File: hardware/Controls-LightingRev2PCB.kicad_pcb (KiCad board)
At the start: 2 copper layers, 54.5 x 53.5 mm, 52 parts, among them IC1 LM74502HDDFR, IC3 ACS724LLCTR-05AU-T, IC4 ACS724LLCTR-05AU-T, IC5 TLV70433DBVT, IC6 ACS724LLCTR-05AU-T, J1 53307-2471, J3 Conn_02x05_Top_Bottom, J4 Conn_01x02, J5 Conn_01x02, J6 Conn_01x03, Q1 NVMFWS1D7N04XMT1G, Q3 IRLML0030, Q4 NVMFWS1D7N04XMT1G, Q5 IRLML0030, U5 SN74LV1T34DBV

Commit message: Layout Review
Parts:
- moved 24V_TP1 93.4 mm to (224.9, 104.7)
- moved LVGND_TP1 86.5 mm to (219.1, 89.3)
- moved GPIO_Addr5v2 73.8 mm to (215.9, 135.3), turned to 90 degrees
- moved GPIO_BPS2 70.4 mm to (208.0, 136.0), turned to 90 degrees
- moved GPIO_Norm1 68.1 mm to (201.8, 135.7), turned to 90 degrees
- moved BPS_Sense2 67.0 mm to (224.0, 119.7), turned to -90 degrees
- moved Norm_Sense1 51.7 mm to (224.0, 112.3), turned to -90 degrees
- moved Addr_Sense2 50.4 mm to (220.9, 93.5)
- moved C24 41.2 mm to (226.7, 96.6), turned to 0 degrees
- moved C21 35.1 mm to (225.9, 99.9), turned to -90 degrees
- moved IC6 32.3 mm to (221.3, 98.6), turned to 0 degrees
- moved C20 29.6 mm to (216.7, 98.7), turned to 90 degrees
- moved C3 20.6 mm to (219.6, 111.0), turned to 0 degrees
- moved C2 16.3 mm to (218.8, 114.3), turned to -90 degrees
- moved R15 13.9 mm to (210.9, 132.7), turned to 0 degrees
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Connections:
- J1 pad 11: ADDR_Sense -> NORMAL_Sense
- J1 pad 13: NORMAL_Sense -> BPS_Sense
- J1 pad 15: BPS_Sense -> GPIO_Addr
- J1 pad 9: GPIO_Addr -> ADDR_Sense
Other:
- outline, holes or cut-outs redrawn

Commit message: Some routing
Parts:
- moved Addr_Sense2 36.3 mm to (232.9, 127.7)
- moved C20 30.1 mm to (213.5, 128.6)
- moved C24 30.1 mm to (223.4, 126.6)
- moved C21 30.1 mm to (222.7, 129.9)
- moved IC6 30.1 mm to (218.1, 128.6)
- moved C15 13.9 mm to (215.2, 108.3)
- moved R12 13.4 mm to (202.0, 109.7)
- moved C12 13.4 mm to (206.0, 106.4)
- moved C17 13.4 mm to (216.0, 105.7)
- moved IC4 13.4 mm to (210.6, 107.7)
- moved Q5 13.4 mm to (204.8, 109.7)
- moved R7 12.6 mm to (219.6, 95.5), turned to 0 degrees
- moved BPS_Sense2 12.4 mm to (224.1, 107.3)
- moved LVPWR1 10.8 mm to (221.9, 96.3), turned to 90 degrees
- moved C6 9.29 mm to (219.5, 97.1), turned to 0 degrees
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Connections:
- 24V_TP1 pad 1: Addressable_PWR -> +24V
- C1 pad 1: Addressable_GND -> GND
- C10 pad 1: Addressable_GND -> GND
- C10 pad 2: Addressable_PWR -> +24V
- C12 pad 1: Addressable_GND -> GND
- C12 pad 2: Addressable_PWR -> +24V
- C15 pad 2: Addressable_GND -> GND
- C17 pad 2: Addressable_GND -> GND
- C19 pad 1: Addressable_GND -> GND
- C2 pad 2: Addressable_GND -> GND
- C20 pad 1: Addressable_GND -> GND
- C20 pad 2: Addressable_PWR -> +24V
- C21 pad 2: Addressable_GND -> GND
- C22 pad 1: Addressable_GND -> GND
- C22 pad 2: Addressable_PWR -> +24V
- C23 pad 1: Addressable_GND -> GND
- C24 pad 2: Addressable_GND -> GND
- C3 pad 2: Addressable_GND -> GND
- C4 pad 2: Addressable_GND -> GND
- C6 pad 1: Addressable_PWR -> +24V
- C6 pad 2: Addressable_GND -> GND
- C7 pad 1: Addressable_PWR -> +24V
- C7 pad 2: Addressable_GND -> GND
- C8 pad 1: Addressable_PWR -> +24V
- C8 pad 2: Addressable_GND -> GND
- C9 pad 2: Addressable_GND -> GND
- D1 pad 2: Addressable_GND -> GND
- IC1 pad 2: Addressable_GND -> GND
- IC3 pad 1: Addressable_PWR -> +24V
- IC3 pad 2: Addressable_PWR -> +24V
- IC3 pad 3: Normal_GND -> Net-(IC3-IP-_1)
- IC3 pad 4: Normal_GND -> Net-(IC3-IP-_1)
- IC3 pad 5: Addressable_GND -> GND
- IC4 pad 1: Addressable_PWR -> +24V
- IC4 pad 2: Addressable_PWR -> +24V
- IC4 pad 3: Strobe_GND -> Net-(IC4-IP-_1)
- IC4 pad 4: Strobe_GND -> Net-(IC4-IP-_1)
- IC4 pad 5: Addressable_GND -> GND
- IC5 pad 1: Addressable_GND -> GND
- IC5 pad 2: Addressable_PWR -> +24V
- IC6 pad 1: Addressable_PWR -> +24V
- IC6 pad 2: Addressable_PWR -> +24V
- IC6 pad 3: Addressable_GND -> Net-(IC6-IP-_1)
- IC6 pad 4: Addressable_GND -> Net-(IC6-IP-_1)
- IC6 pad 5: Addressable_GND -> GND
- J1 pad 1: Addressable_GND -> GND
- J1 pad 24: Addressable_PWR -> +24V
- J1 pad 3: Addressable_GND -> GND
- J1 pad 5: Addressable_GND -> GND
- J3 pad 10: Addressable_GND -> GND
- J3 pad 4: Addressable_GND -> GND
- J3 pad 5: Addressable_GND -> GND
- J3 pad 9: Addressable_GND -> GND
- J4 pad 1: Addressable_PWR -> Net-(IC4-IP-_1)
- J4 pad 2: Strobe_GND -> Net-(J4-Pin_2)
- J5 pad 1: Addressable_PWR -> Net-(IC3-IP-_1)
- J5 pad 2: Normal_GND -> Net-(J5-Pin_2)
- J6 pad 1: Addressable_PWR -> Net-(IC6-IP-_1)
- J6 pad 2: Addressable_GND -> GND
- LVGND_TP1 pad 1: Addressable_GND -> GND
- LVPWR1 pad 1: Addressable_GND -> GND
- Q3 pad 2: Addressable_GND -> GND
- Q3 pad 3: Normal_GND -> Net-(J5-Pin_2)
- Q4 pad 5: Addressable_PWR -> +24V
- Q4 pad 6: Addressable_PWR -> +24V
- Q4 pad 7: Addressable_PWR -> +24V
- Q4 pad 8: Addressable_PWR -> +24V
- Q4 pad 9: Addressable_PWR -> +24V
- Q5 pad 2: Addressable_GND -> GND
- Q5 pad 3: Strobe_GND -> Net-(J4-Pin_2)
- R11 pad 1: Addressable_GND -> GND
- R12 pad 1: Addressable_GND -> GND
- R6 pad 2: Addressable_GND -> GND
- R7 pad 1: Addressable_PWR -> +24V
- U5 pad 3: Addressable_GND -> GND
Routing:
- net GND: track 0.00 -> 78.8 mm, vias 0 -> 20
- net GPIO_Normal: track 0.00 -> 37.4 mm, vias 0 -> 8
- net Net-(IC6-IP-_1): track 0.00 -> 32.9 mm, vias 0 -> 5
- net Net-(IC3-IP-_1): track 0.00 -> 30.6 mm, vias 0 -> 4
- net Addressable_Logic: track 0.00 -> 30.0 mm, vias 0 -> 4
- net Net-(IC4-IP-_1): track 0.00 -> 27.2 mm, vias 0 -> 4
- net Net-(J5-Pin_2): track 0.00 -> 26.1 mm, vias 0 -> 4
- net CAN_H: track 0.00 -> 25.8 mm, vias 0 -> 4
- net CAN_L: track 0.00 -> 25.1 mm, vias 0 -> 4
- net GPIO_BPS_Strobe: track 0.00 -> 25.0 mm, vias 0 -> 4
- net 24V_EXT: track 0.00 -> 23.3 mm, vias 0 -> 2
- net Net-(IC1-SRC): track 0.00 -> 23.1 mm, vias 0 -> 4
- net Net-(J4-Pin_2): track 0.00 -> 22.2 mm, vias 0 -> 4
- net Net-(IC1-GATE): track 0.00 -> 21.2 mm, vias 0 -> 2
- net /Reverse Polarity Protection/RPP_EN: track 0.00 -> 20.1 mm, vias 0 -> 2
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- added copper zone on F.Cu, net +24V
- added copper zone on B.Cu, net GND
- added copper zone on F.Cu, net GND
- removed copper zone on B.Cu, net Addressable_GND
- removed copper zone on F.Cu, net Addressable_PWR
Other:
- outline, holes or cut-outs redrawn

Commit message: Layout Review
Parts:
- removed Addr_Sense2, BPS_Sense2, Norm_Sense1: TestPoint, UTSVT_Special:TestPoint_HEX_3mmID
- added Addr_Sense: TestPoint, UTSVT_Special:TestPoint_HEX_3mmID, F.Cu at (221.6, 94.3)
- added BPS_Sense: TestPoint, UTSVT_Special:TestPoint_HEX_3mmID, F.Cu at (221.6, 104.6)
- added G***: LHRs_LOGO, UTSVT_Logos:LHRs_LOGO, F.Cu at (193.4, 116.0)
- added Norm_Sense: TestPoint, UTSVT_Special:TestPoint_HEX_3mmID, F.Cu at (221.6, 99.4)
- moved GPIO_BPS2 46.6 mm to (200.2, 89.4)
- moved LVGND_TP1 45.9 mm to (208.6, 136.0), turned to 90 degrees
- moved 24V_TP1 27.8 mm to (223.8, 127.8)
- moved Q3 15.9 mm to (192.8, 119.9), turned to 180 degrees
- moved C21 14.1 mm to (208.7, 131.1)
- moved IC6 14.1 mm to (204.1, 129.9)
- moved C24 14.1 mm to (209.4, 127.8)
- moved C3 13.2 mm to (209.4, 120.5)
- moved IC3 13.2 mm to (204.1, 122.5)
- moved C20 13.1 mm to (200.6, 126.3), turned to 0 degrees
- moved C2 13.1 mm to (208.7, 123.6)
- moved Q5 12.3 mm to (192.8, 112.5), turned to 180 degrees
- moved C7 11.5 mm to (211.5, 107.1)
- moved C8 11.5 mm to (211.5, 108.7)
- moved R7 11.5 mm to (211.5, 103.7)
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- renumbered GPIO_Norm1 to GPIO_Norm
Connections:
- net GPIO_Addr renamed GPIO_3v3Addr
- C17 pad 1: 5V PWR -> +3.3V
- C24 pad 1: 5V PWR -> +3.3V
- C3 pad 1: 5V PWR -> +3.3V
- IC3 pad 8: 5V PWR -> +3.3V
- IC4 pad 8: 5V PWR -> +3.3V
- IC6 pad 8: 5V PWR -> +3.3V
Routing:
- net ADDR_Sense: track 0.00 -> 74.8 mm, vias 0 -> 2
- net NORMAL_Sense: track 0.00 -> 64.1 mm, vias 0 -> 2
- net BPS_Sense: track 0.00 -> 55.5 mm, vias 0 -> 2
- net GPIO_3v3Addr: track 0.00 -> 49.4 mm, vias 0 -> 2
- net +3.3V: track 0.00 -> 47.4 mm, vias 0 -> 6
- net GPIO_Normal: track 37.4 -> 81.0 mm, vias 8 -> 6
- net Net-(IC3-IP-_1): track 30.6 -> 0.00 mm, vias 4 -> 0
- net Net-(IC4-IP-_1): track 27.2 -> 0.00 mm, vias 4 -> 0
- net GND: track 78.8 -> 54.0 mm, vias 20 -> 29
- net Net-(C4-Pad1): track 20.1 -> 0.00 mm, vias 2 -> 0
- net GPIO_BPS_Strobe: track 25.0 -> 44.8 mm
- net Net-(J5-Pin_2): track 26.1 -> 7.20 mm, vias 4 -> 0
- net Net-(IC1-SRC): track 23.1 -> 5.96 mm, vias 4 -> 2
- net Net-(J4-Pin_2): track 22.2 -> 6.88 mm, vias 4 -> 0
- net Net-(IC6-IP-_1): track 32.9 -> 17.9 mm, vias 5 -> 0
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- added copper zone on F.Cu, net 24V_EXT
- added copper zone on F.Cu, net Net-(C4-Pad1)
- added copper zone on F.Cu, net Net-(IC1-SRC)
- added copper zone on F.Cu, net Net-(IC3-IP-_1)
- added copper zone on F.Cu, net Net-(IC4-IP-_1)
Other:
- board text added: "Eliana Tejeda LHRS 2025-2026"
- board text added: "Lighting Board"

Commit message: Ready for Layout Review
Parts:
- renumbered 24V_TP1 to 24V_TP, GPIO_Addr5v2 to GPIO_Addr5v, LVGND_TP1 to LVGND_TP
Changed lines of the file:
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@@
 		(layer "F.Cu")
 		(at 208.6356 136.0424 90)
-		(property "Reference" "LVGND_TP1"
+		(property "Reference" "LVGND_TP"
 			(at 2.54 0 0)
 			(unlocked yes)
@@
 		(layer "F.Cu")
 		(at 215.85 136.0932 90)
-		(property "Reference" "GPIO_Addr5v2"
+		(property "Reference" "GPIO_Addr5v"
 			(at 2.5654 0.0246 0)
 			(unlocked yes)
@@
 		(layer "F.Cu")
 		(at 223.75 127.75 -90)
-		(property "Reference" "24V_TP1"
-			(at 2.25 0 0)
+		(property "Reference" "24V_TP"
+			(at 2.65 0.05 0)
 			(unlocked yes)
 			(layer "F.SilkS")

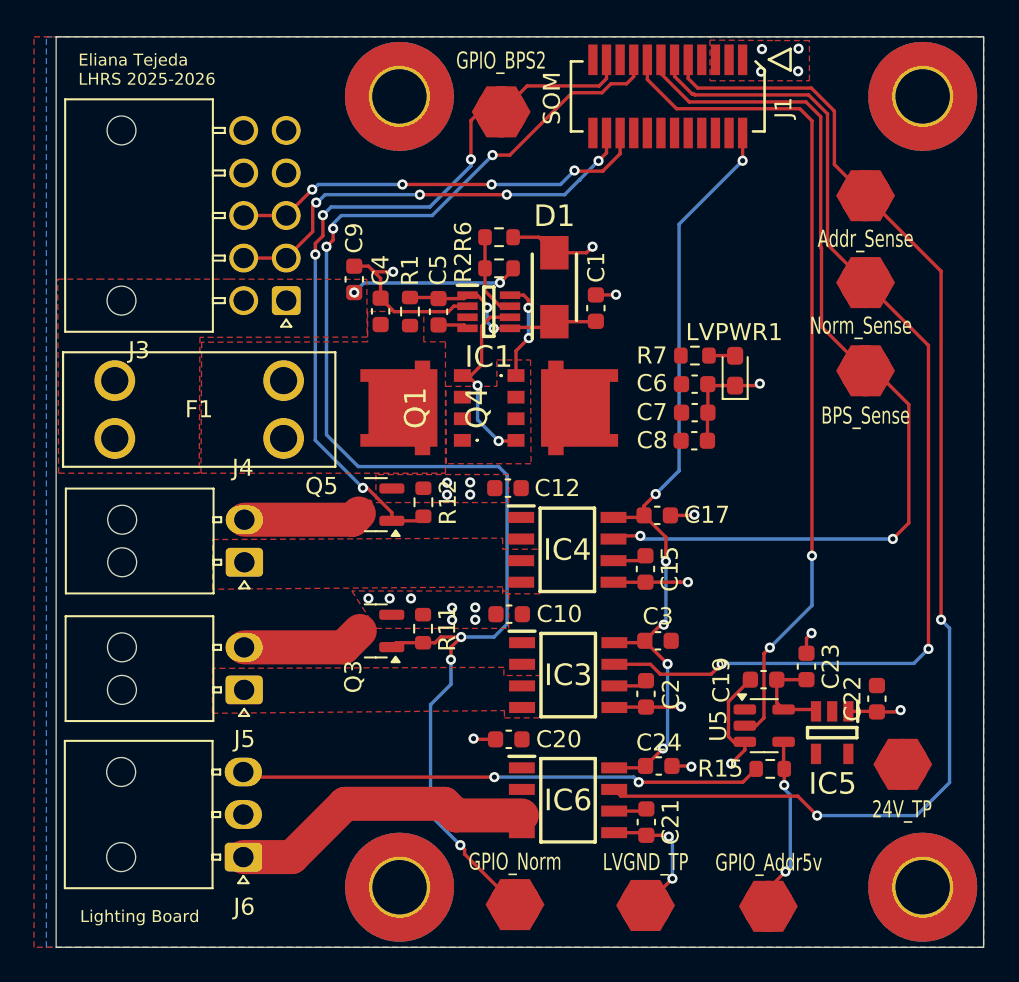
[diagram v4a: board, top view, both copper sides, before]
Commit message: All review requests escept LDO addressed
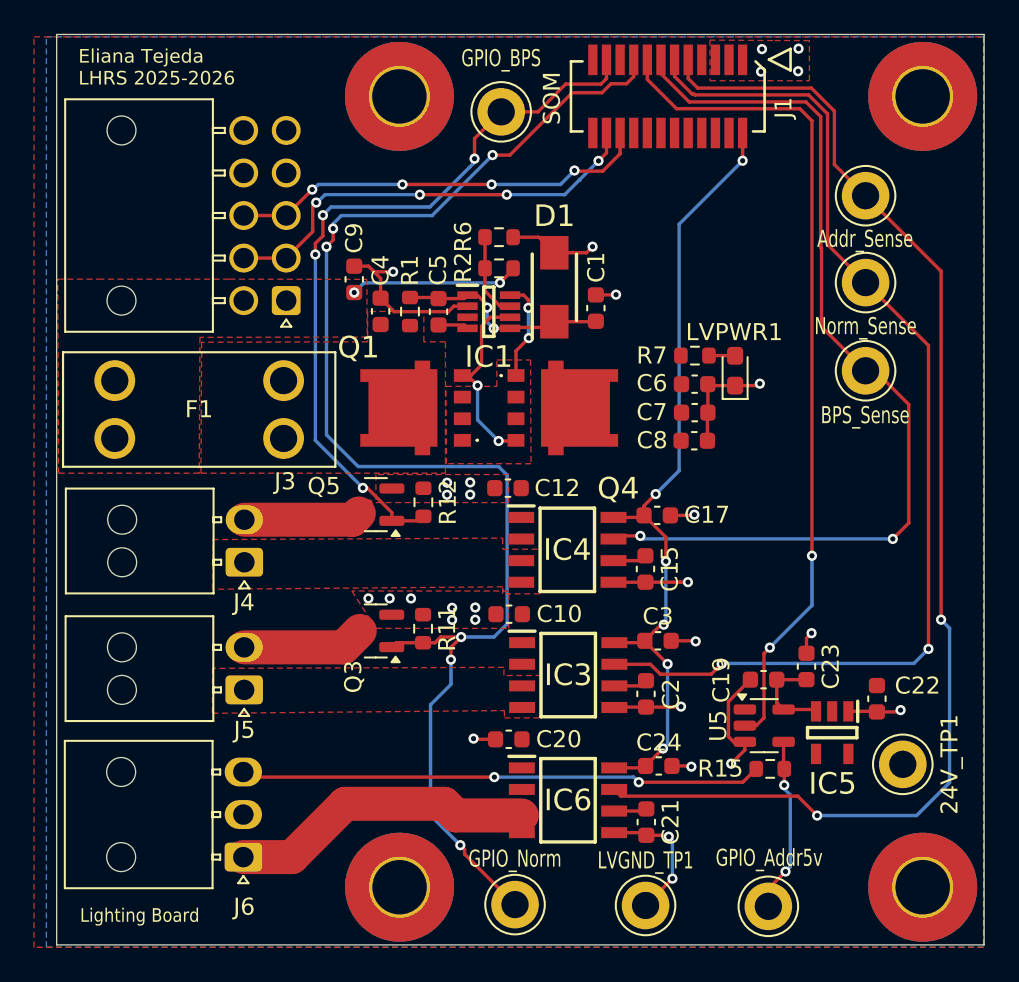
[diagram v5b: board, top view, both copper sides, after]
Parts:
- 24V_TP1: renamed from 24V_TP; footprint UTSVT_Special:TestPoint_HEX_3mmID -> TestPoint:TestPoint_Keystone_5005-5009_Compact
- Addr_Sense, BPS_Sense, GPIO_Addr5v, GPIO_Norm, Norm_Sense: footprint UTSVT_Special:TestPoint_HEX_3mmID -> TestPoint:TestPoint_Keystone_5005-5009_Compact
- GPIO_BPS: renamed from GPIO_BPS2; footprint UTSVT_Special:TestPoint_HEX_3mmID -> TestPoint:TestPoint_Keystone_5005-5009_Compact
- LVGND_TP1: renamed from LVGND_TP; footprint UTSVT_Special:TestPoint_HEX_3mmID -> TestPoint:TestPoint_Keystone_5005-5009_Compact
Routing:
- net GND: track 54.0 -> 55.5 mm, vias 29 -> 30
- net GPIO_BPS_Strobe: track 44.8 -> 44.0 mm
